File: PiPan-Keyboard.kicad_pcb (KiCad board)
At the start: 2 copper layers, 260.3 x 76.2 mm, 101 parts, among them J0 Conn_01x18_MountingPin, SW0 RotaryEncoder_Switch, U1 Pico

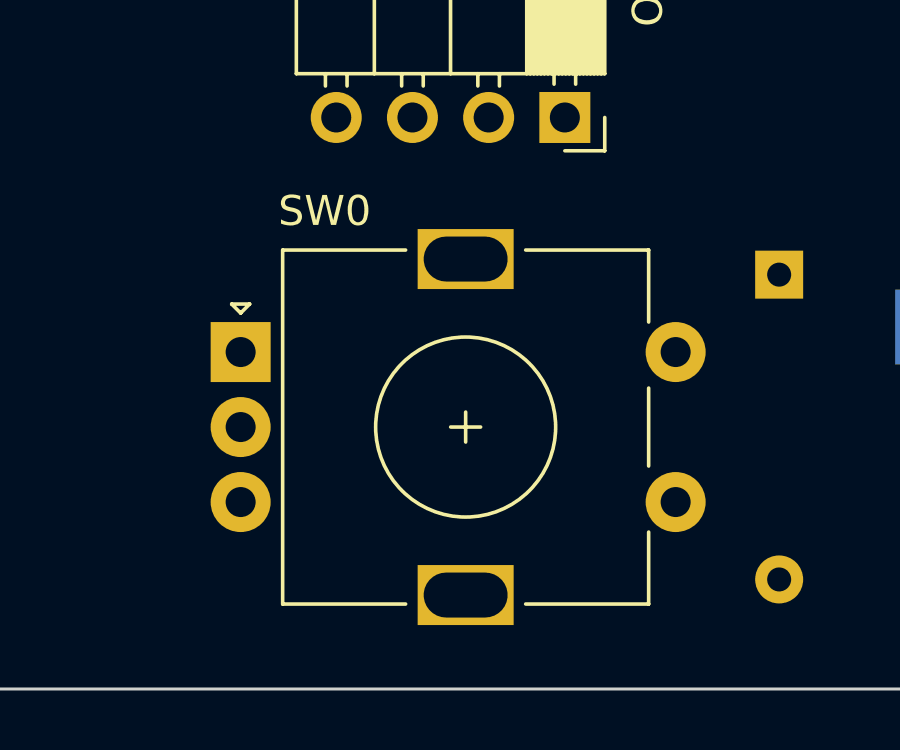
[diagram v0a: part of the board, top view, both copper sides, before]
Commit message: moved encoder and updated .step
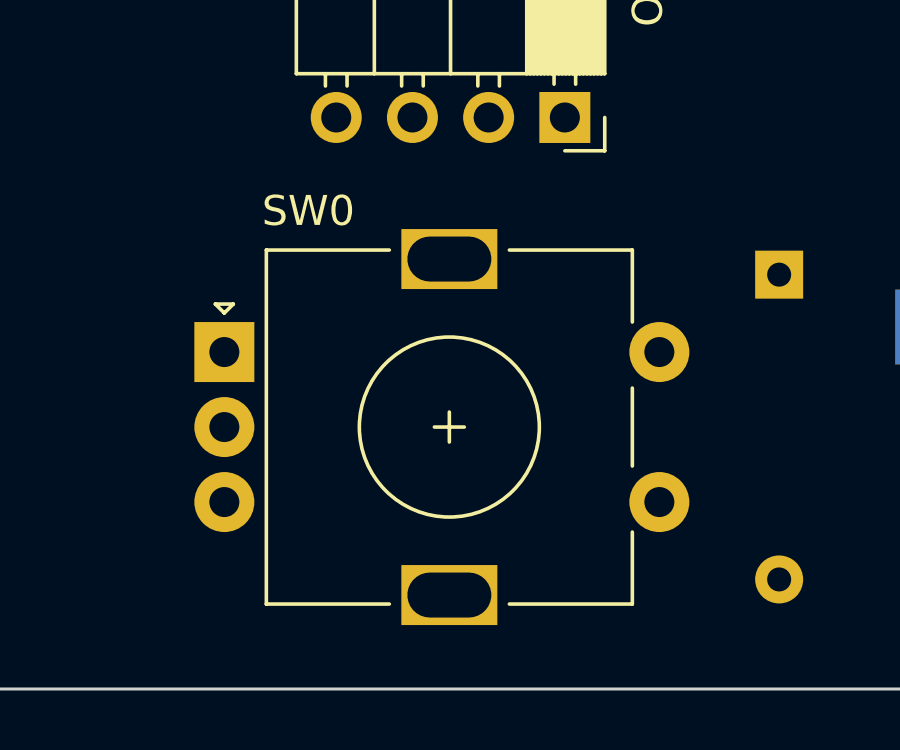
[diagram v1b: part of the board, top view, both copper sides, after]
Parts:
- moved SW0 0.54 mm to (37.1, 126.1)
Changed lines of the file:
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@@
   )
   (footprint "Rotary_Encoder:RotaryEncoder_Alps_EC11E-Switch_Vertical_H20mm" (layer "F.Cu")
-    (at 37.6125 126.0875)
+    (at 37.06875 126.0875)
     (descr "Alps rotary encoder, EC12E... with switch, vertical shaft, http://www.alps.com/prod/info/E/HTML/Encoder/Incremental/EC11/EC11E15204A3.html")
     (tags "rotary encoder")

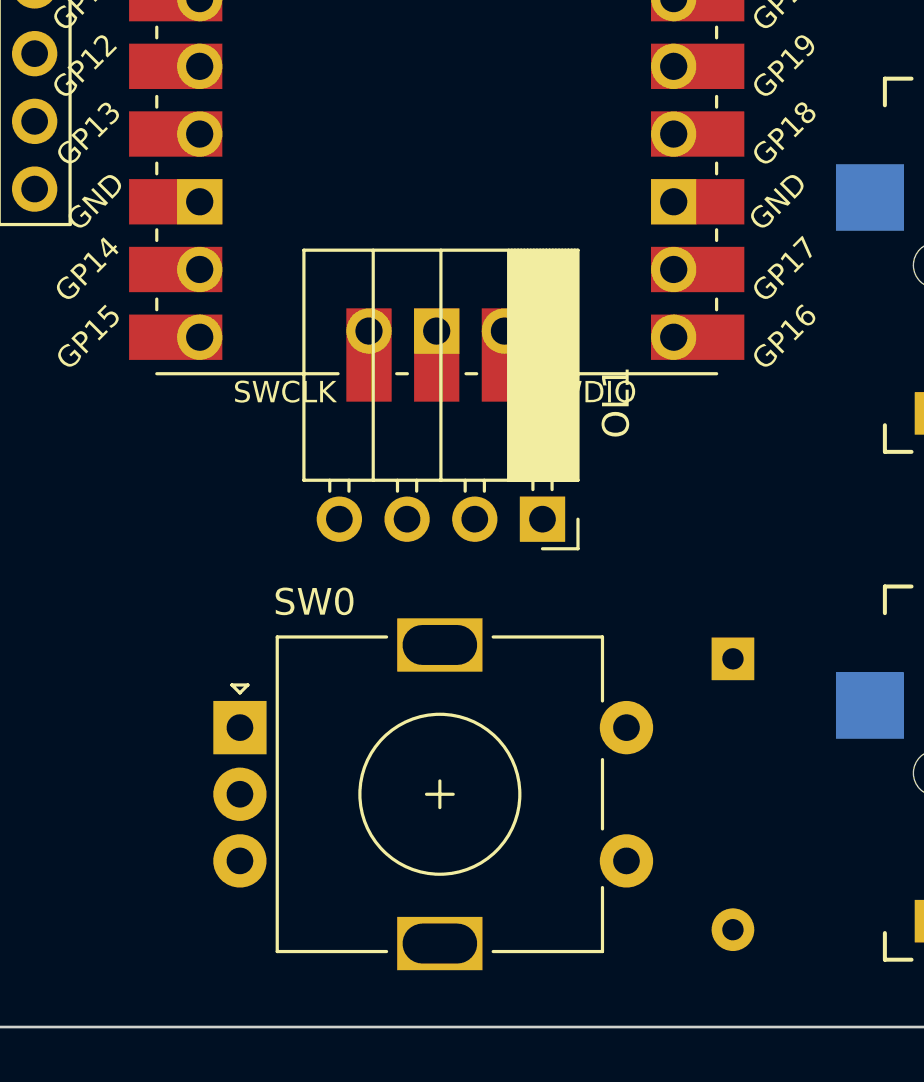
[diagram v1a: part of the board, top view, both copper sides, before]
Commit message: moved encoder
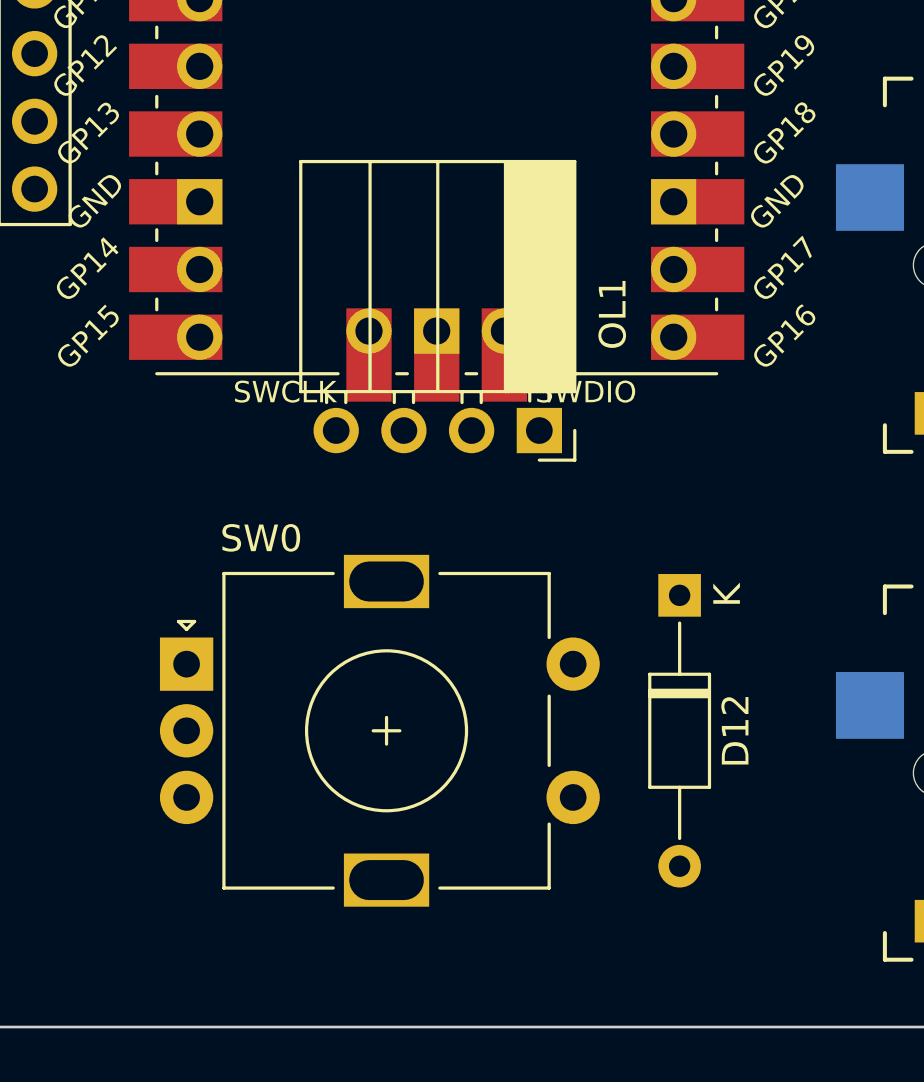
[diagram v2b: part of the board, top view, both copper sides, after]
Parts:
- D12: moved to F.Cu
- moved OL1 3.33 mm to (48.3, 114.9)
- moved SW0 3.11 mm to (35.1, 123.7)
- moved D12 3.11 mm to (53.6, 121.1)
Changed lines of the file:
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@@
       (net 59 "Net-(D36-Pad2)") (pinfunction "ROW") (pintype "passive"))
   )
+  (footprint "Diode_THT:D_DO-35_SOD27_P10.16mm_Horizontal" (layer "F.Cu")
+    (at 53.5625 121.12625 -90)
+    (descr "Diode, DO-35_SOD27 series, Axial, Horizontal, pin pitch=10.16mm, , length*diameter=4*2mm^2, , http://www.diodes.com/_files/packages/DO-35.pdf")
+    (tags "Diode DO-35_SOD27 series Axial Horizontal pin pitch 10.16mm  length 4mm diameter 2mm")
+    (property "Sheetfile" "PiPan-Keyboard.kicad_sch")
+    (property "Sheetname" "")
+    (attr through_hole)
+    (fp_text reference "D12" (at 5.08 -2.12 90) (layer "F.SilkS")
+      (effects (font (size 1 1) (thickness 0.15)))
+    )
+    (fp_text value "D_Small" (at 5.08 2.12 90) (layer "F.Fab")
+      (effects (font (size 1 1) (thickness 0.15)))
+    )
+    (fp_text user "K" (at 0 -1.8 90) (layer "F.SilkS")
+      (effects (font (size 1 1) (thickness 0.15)))
+    )
+    (fp_text user "K" (at 0 -1.8 90) (layer "F.Fab")
+      (effects (font (size 1 1) (thickness 0.15)))
+    )
+    (fp_text user "${REFERENCE}" (at 5.38 0 90) (layer "F.Fab")
+      (effects (font (size 0.8 0.8) (thickness 0.12)))
+    )
+    (fp_line (start 2.96 1.12) (end 7.2 1.12) (layer "F.SilkS") (width 0.12))
+    (fp_line (start 1.04 0) (end 2.96 0) (layer "F.SilkS") (width 0.12))
+    (fp_line (start 9.12 0) (end 7.2 0) (layer "F.SilkS") (width 0.12))
+    (fp_line (start 7.2 1.12) (end 7.2 -1.12) (layer "F.SilkS") (width 0.12))
+    (fp_line (start 3.56 -1.12) (end 3.56 1.12) (layer "F.SilkS") (width 0.12))
+    (fp_line (start 3.8 -1.12) (end 3.8 1.12) (layer "F.SilkS") (width 0.12))
+    (fp_line (start 7.2 -1.12) (end 2.96 -1.12) (layer "F.SilkS") (width 0.12))
+    (fp_line (start 3.68 -1.12) (end 3.68 1.12) (layer "F.SilkS") (width 0.12))
+    (fp_line (start 2.96 -1.12) (end 2.96 1.12) (layer "F.SilkS") (width 0.12))
+    (fp_line (start -1.05 -1.25) (end -1.05 1.25) (layer "F.CrtYd") (width 0.05))
+    (fp_line (start -1.05 1.25) (end 11.21 1.25) (layer "F.CrtYd") (width 0.05))
+    (fp_line (start 11.21 -1.25) (end -1.05 -1.25) (layer "F.CrtYd") (width 0.05))
+    (fp_line (start 11.21 1.25) (end 11.21 -1.25) (layer "F.CrtYd") (width 0.05))
+    (fp_line (start 3.08 1) (end 7.08 1) (layer "F.Fab") (width 0.1))
+    (fp_line (start 10.16 0) (end 7.08 0) (layer "F.Fab") (width 0.1))
+    (fp_line (start 3.68 -1) (end 3.68 1) (layer "F.Fab") (width 0.1))
+    (fp_line (start 3.08 -1) (end 3.08 1) (layer "F.Fab") (width 0.1))
+    (fp_line (start 3.58 -1) (end 3.58 1) (layer "F.Fab") (width 0.1))
+    (fp_line (start 7.08 1) (end 7.08 -1) (layer "F.Fab") (width 0.1))
+    (fp_line (start 3.78 -1) (end 3.78 1) (layer "F.Fab") (width 0.1))
+    (fp_line (start 0 0) (end 3.08 0) (layer "F.Fab") (width 0.1))
+    (fp_line (start 7.08 -1) (end 3.08 -1) (layer "F.Fab") (width 0.1))
+    (pad "1" thru_hole rect (at 0 0 270) (size 1.6 1.6) (drill 0.8) (layers *.Cu *.Mask)
+      (net 1 "ROW0") (pinfunction "K") (pintype "passive"))
+    (pad "2" thru_hole oval (at 10.16 0 270) (size 1.6 1.6) (drill 0.8) (layers *.Cu *.Mask)
+      (net 45 "Net-(D12-Pad2)") (pinfunction "A") (pintype "passive"))
+    (model "${KICAD6_3DMODEL_DIR}/Diode_THT.3dshapes/D_DO-35_SOD27_P10.16mm_Horizontal.wrl"
+      (offset (xyz 0 0 0))
+      (scale (xyz 1 1 1))
+      (rotate (xyz 0 0 0))
+    )
+  )
   (footprint "keyswitches:Kailh_socket_MX-Outlined" (layer "F.Cu")
     (at 239.7125 127.79375)
@@
   )
   (footprint "Connector_PinSocket_2.54mm:PinSocket_1x04_P2.54mm_Horizontal" (layer "F.Cu")
-    (at 48.41875 118.26875 -90)
+    (at 48.3 114.94375 -90)
     (descr "Through hole angled socket strip, 1x04, 2.54mm pitch, 8.51mm socket length, single row (from Kicad 4.0.7), script generated")
     (tags "Through hole angled socket strip THT 1x04 2.54mm single row")
@@
   )
   (footprint "Rotary_Encoder:RotaryEncoder_Alps_EC11E-Switch_Vertical_H20mm" (layer "F.Cu")
-    (at 37.06875 126.0875)
+    (at 35.06875 123.70625)
     (descr "Alps rotary encoder, EC12E... with switch, vertical shaft, http://www.alps.com/prod/info/E/HTML/Encoder/Incremental/EC11/EC11E15204A3.html")
     (tags "rotary encoder")
@@
     (model "${KICAD6_3DMODEL_DIR}/Diode_THT.3dshapes/D_DO-35_SOD27_P10.16mm_Horizontal.wrl"
       (offset (xyz 0 0 0))
-      (scale (xyz 1 1 1))
-      (rotate (xyz 0 0 0))
-    )
-  )
-  (footprint "Diode_THT:D_DO-35_SOD27_P10.16mm_Horizontal" (layer "B.Cu")
-    (at 55.5625 123.5075 -90)
-    (descr "Diode, DO-35_SOD27 series, Axial, Horizontal, pin pitch=10.16mm, , length*diameter=4*2mm^2, , http://www.diodes.com/_files/packages/DO-35.pdf")
-    (tags "Diode DO-35_SOD27 series Axial Horizontal pin pitch 10.16mm  length 4mm diameter 2mm")
-    (property "Sheetfile" "PiPan-Keyboard.kicad_sch")
-    (property "Sheetname" "")
-    (attr through_hole)
-    (fp_text reference "D12" (at 5.08 2.12 -270) (layer "B.SilkS")
-      (effects (font (size 1 1) (thickness 0.15)) (justify mirror))
-    )
-    (fp_text value "D_Small" (at 5.08 -2.12 -270) (layer "B.Fab")
-      (effects (font (size 1 1) (thickness 0.15)) (justify mirror))
-    )
-    (fp_text user "K" (at 0 1.8 -270) (layer "B.SilkS")
-      (effects (font (size 1 1) (thickness 0.15)) (justify mirror))
-    )
-    (fp_text user "K" (at 0 1.8 -270) (layer "B.Fab")
-      (effects (font (size 1 1) (thickness 0.15)) (justify mirror))
-    )
-    (fp_text user "${REFERENCE}" (at 5.38 0 -270) (layer "B.Fab")
-      (effects (font (size 0.8 0.8) (thickness 0.12)) (justify mirror))
-    )
-    (fp_line (start 2.96 -1.12) (end 7.2 -1.12) (layer "B.SilkS") (width 0.12))
-    (fp_line (start 1.04 0) (end 2.96 0) (layer "B.SilkS") (width 0.12))
-    (fp_line (start 9.12 0) (end 7.2 0) (layer "B.SilkS") (width 0.12))
-    (fp_line (start 7.2 -1.12) (end 7.2 1.12) (layer "B.SilkS") (width 0.12))
-    (fp_line (start 3.56 1.12) (end 3.56 -1.12) (layer "B.SilkS") (width 0.12))
-    (fp_line (start 3.8 1.12) (end 3.8 -1.12) (layer "B.SilkS") (width 0.12))
-    (fp_line (start 7.2 1.12) (end 2.96 1.12) (layer "B.SilkS") (width 0.12))
-    (fp_line (start 3.68 1.12) (end 3.68 -1.12) (layer "B.SilkS") (width 0.12))
-    (fp_line (start 2.96 1.12) (end 2.96 -1.12) (layer "B.SilkS") (width 0.12))
-    (fp_line (start -1.05 1.25) (end -1.05 -1.25) (layer "B.CrtYd") (width 0.05))
-    (fp_line (start -1.05 -1.25) (end 11.21 -1.25) (layer "B.CrtYd") (width 0.05))
-    (fp_line (start 11.21 1.25) (end -1.05 1.25) (layer "B.CrtYd") (width 0.05))
-    (fp_line (start 11.21 -1.25) (end 11.21 1.25) (layer "B.CrtYd") (width 0.05))
-    (fp_line (start 3.08 -1) (end 7.08 -1) (layer "B.Fab") (width 0.1))
-    (fp_line (start 10.16 0) (end 7.08 0) (layer "B.Fab") (width 0.1))
-    (fp_line (start 3.68 1) (end 3.68 -1) (layer "B.Fab") (width 0.1))
-    (fp_line (start 3.08 1) (end 3.08 -1) (layer "B.Fab") (width 0.1))
-    (fp_line (start 3.58 1) (end 3.58 -1) (layer "B.Fab") (width 0.1))
-    (fp_line (start 7.08 -1) (end 7.08 1) (layer "B.Fab") (width 0.1))
-    (fp_line (start 3.78 1) (end 3.78 -1) (layer "B.Fab") (width 0.1))
-    (fp_line (start 0 0) (end 3.08 0) (layer "B.Fab") (width 0.1))
-    (fp_line (start 7.08 1) (end 3.08 1) (layer "B.Fab") (width 0.1))
-    (pad "1" thru_hole rect (at 0 0 270) (size 1.6 1.6) (drill 0.8) (layers *.Cu *.Mask)
-      (net 1 "ROW0") (pinfunction "K") (pintype "passive"))
-    (pad "2" thru_hole oval (at 10.16 0 270) (size 1.6 1.6) (drill 0.8) (layers *.Cu *.Mask)
-      (net 45 "Net-(D12-Pad2)") (pinfunction "A") (pintype "passive"))
-    (model "${KICAD6_3DMODEL_DIR}/Diode_THT.3dshapes/D_DO-35_SOD27_P10.16mm_Horizontal.wrl"
-      (offset (xyz 0 0 0))

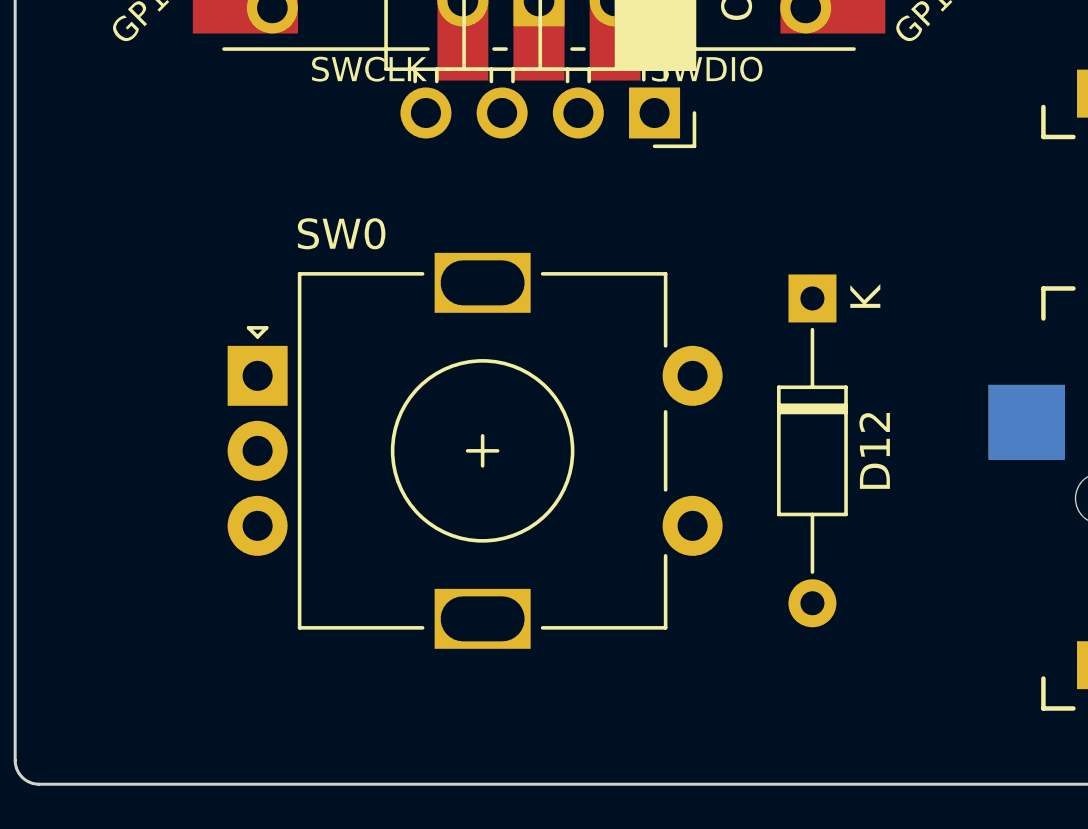
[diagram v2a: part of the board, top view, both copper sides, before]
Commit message: moved encoder again
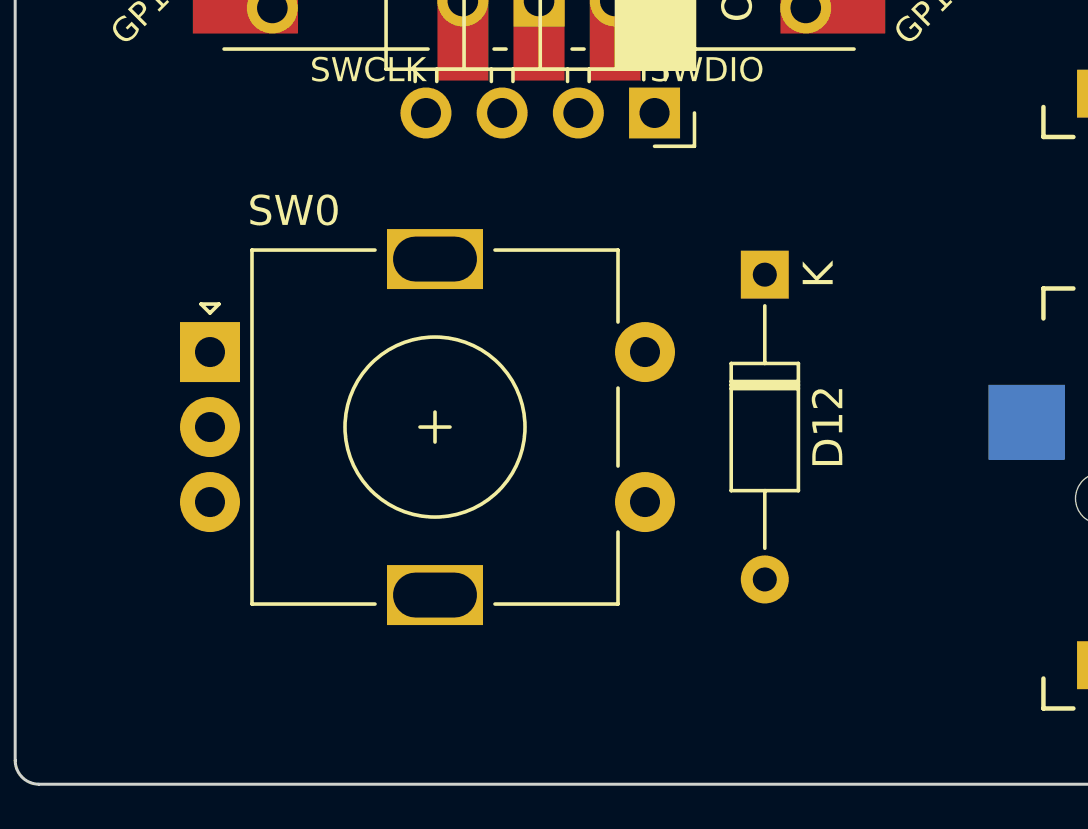
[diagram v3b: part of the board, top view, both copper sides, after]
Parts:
- moved D12 1.77 mm to (52.0, 120.3)
- moved SW0 1.77 mm to (33.5, 122.9)
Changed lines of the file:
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@@
   )
   (footprint "Diode_THT:D_DO-35_SOD27_P10.16mm_Horizontal" (layer "F.Cu")
-    (at 53.5625 121.12625 -90)
+    (at 51.975 120.3325 -90)
     (descr "Diode, DO-35_SOD27 series, Axial, Horizontal, pin pitch=10.16mm, , length*diameter=4*2mm^2, , http://www.diodes.com/_files/packages/DO-35.pdf")
     (tags "Diode DO-35_SOD27 series Axial Horizontal pin pitch 10.16mm  length 4mm diameter 2mm")
@@
   )
   (footprint "Rotary_Encoder:RotaryEncoder_Alps_EC11E-Switch_Vertical_H20mm" (layer "F.Cu")
-    (at 35.06875 123.70625)
+    (at 33.48125 122.9125)
     (descr "Alps rotary encoder, EC12E... with switch, vertical shaft, http://www.alps.com/prod/info/E/HTML/Encoder/Incremental/EC11/EC11E15204A3.html")
     (tags "rotary encoder")

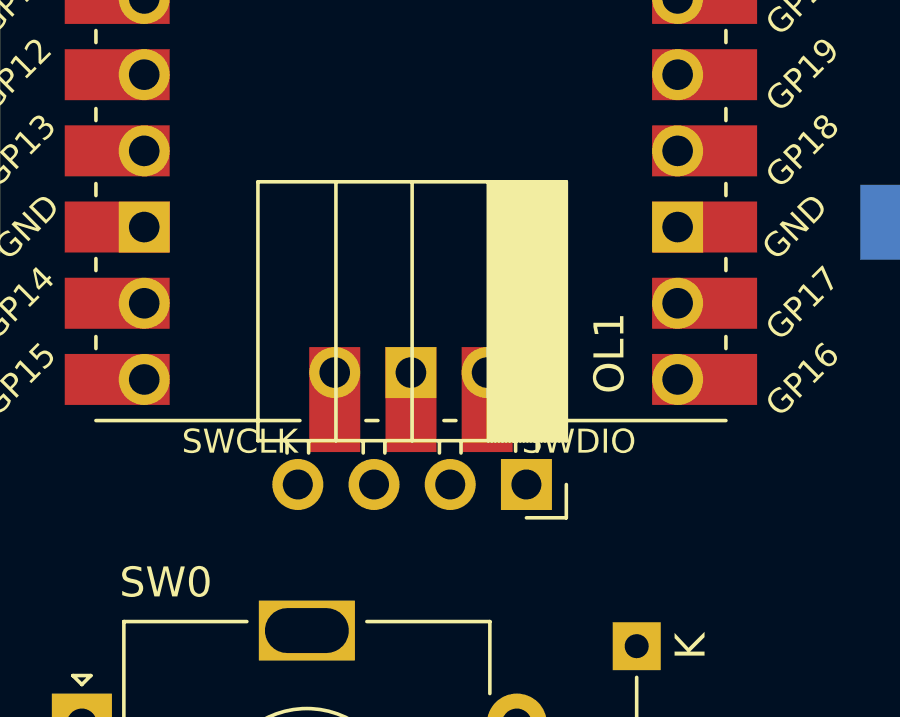
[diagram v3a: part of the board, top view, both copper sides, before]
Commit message: moved OLED and generated new .step
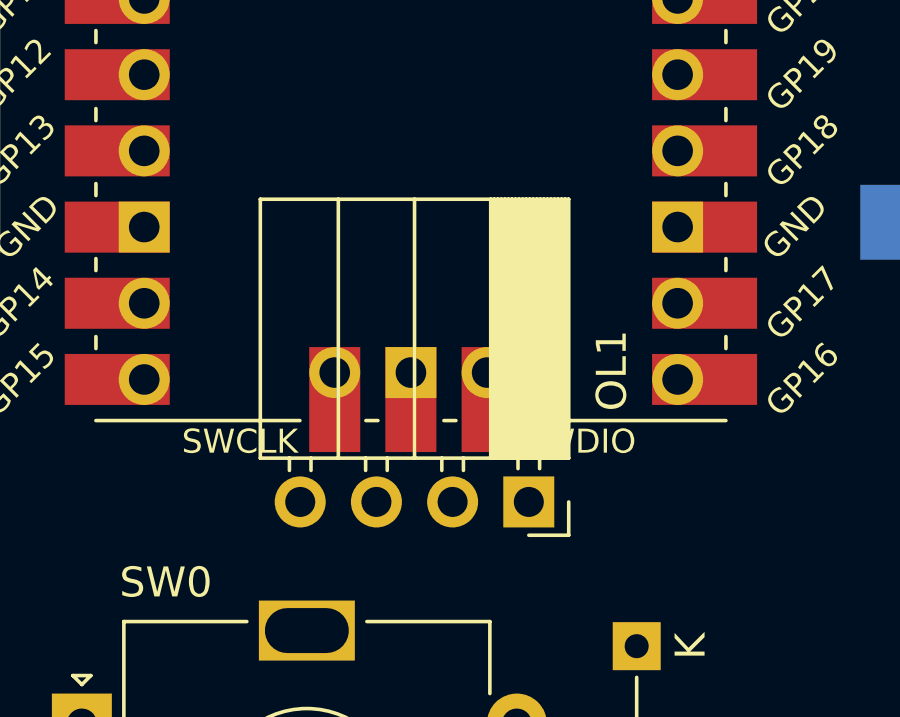
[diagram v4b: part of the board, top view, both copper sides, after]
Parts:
- moved OL1 0.59 mm to (48.4, 115.5)
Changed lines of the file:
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@@
   )
   (footprint "Connector_PinSocket_2.54mm:PinSocket_1x04_P2.54mm_Horizontal" (layer "F.Cu")
-    (at 48.3 114.94375 -90)
+    (at 48.38 115.525 -90)
     (descr "Through hole angled socket strip, 1x04, 2.54mm pitch, 8.51mm socket length, single row (from Kicad 4.0.7), script generated")
     (tags "Through hole angled socket strip THT 1x04 2.54mm single row")
